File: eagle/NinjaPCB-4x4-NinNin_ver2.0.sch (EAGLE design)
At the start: 72 parts, among them IC3 ANALOGSW_AD_SOT23-6, IC6 NAU7802, J2 ATX24, J3 HEATER, J4 HEATER_TEMP, Q1 S8550, Q2 IRF520NPBF, Q3 IRF520NPBF, Q4 S8550, Q5 IRF520NPBF, Q6 S8550, Q7 S8550, Q8 S8550, U1 CJT1117-3.3-SOT223

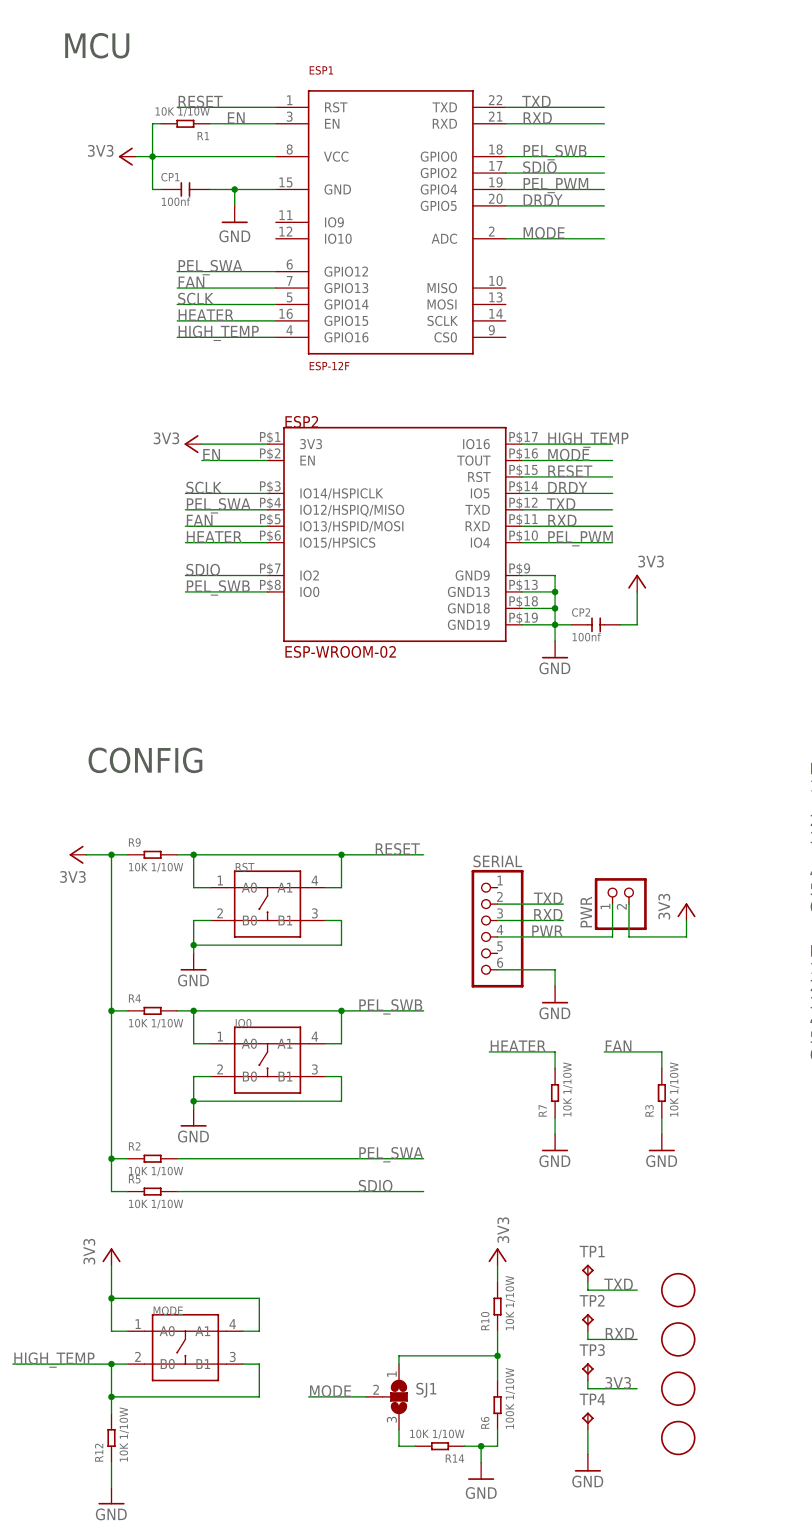
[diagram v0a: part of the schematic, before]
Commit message: abstract layout image of 2x2MooMoo
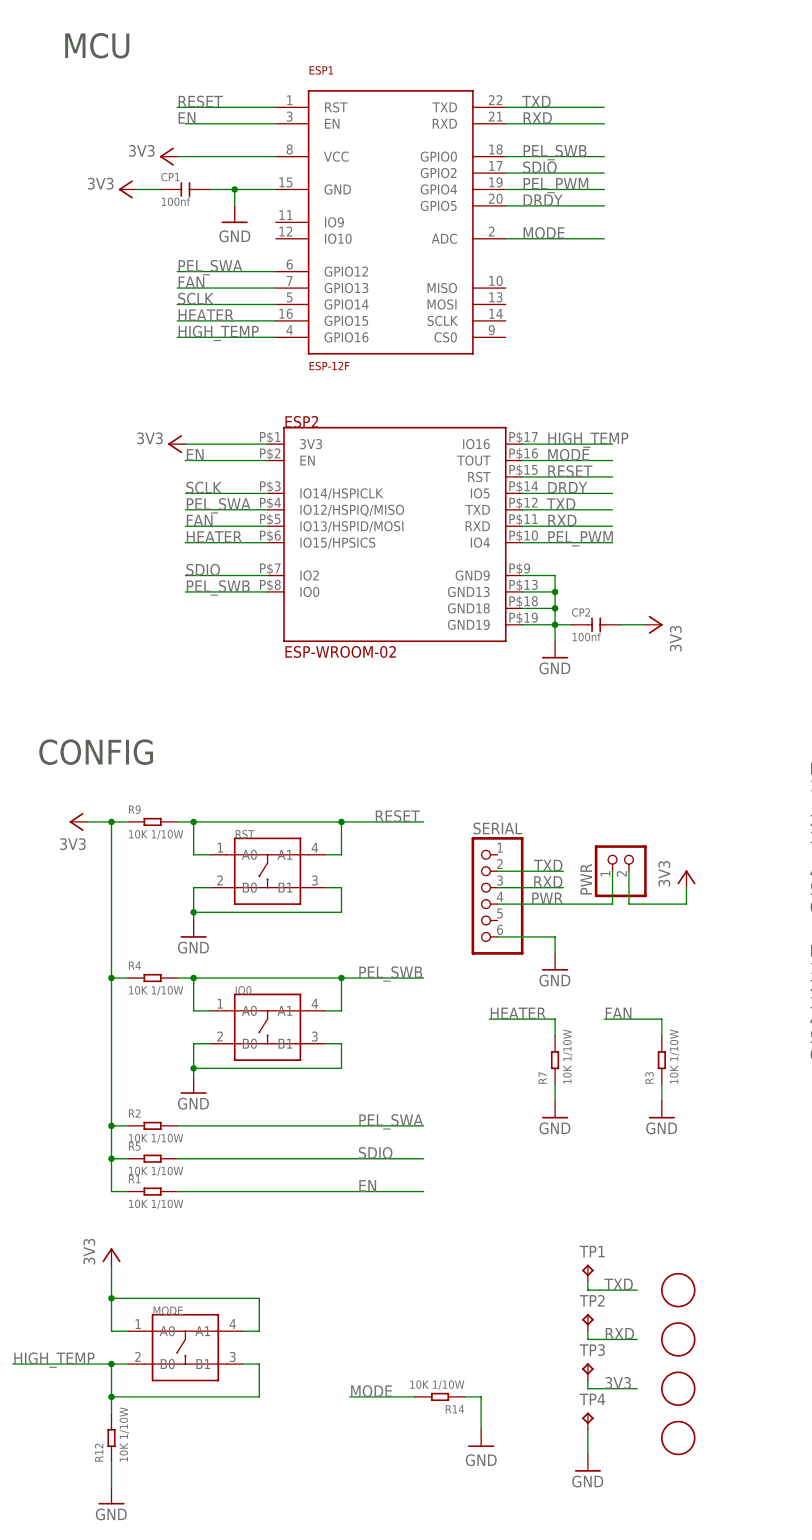
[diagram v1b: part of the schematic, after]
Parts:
- removed R10: 10K 1/10W, Seeed-Resistor:SMD-RES-10K-5%-1/10W(0603)
- removed R6: 100K 1/10W, Seeed-Resistor:SMD-RES-100K-5%-1/10W(0603)
- removed SJ1: (no value), jumper:SJ2W
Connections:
- removed net N$8: R10.1, R6.2, SJ1.1
- removed net N$9: R14.2, SJ1.3
- net 3V3: now also R1.1; no longer R1.2, R10.2
- net EN: now also R1.2; no longer R1.1
- net GND: no longer R6.1
- net MODE: now also R14.2; no longer SJ1.2
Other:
- moved on the sheet: IO0, PWR, R1, R14, R2, R3, R4, R5, R7, R9, RST, SERIAL

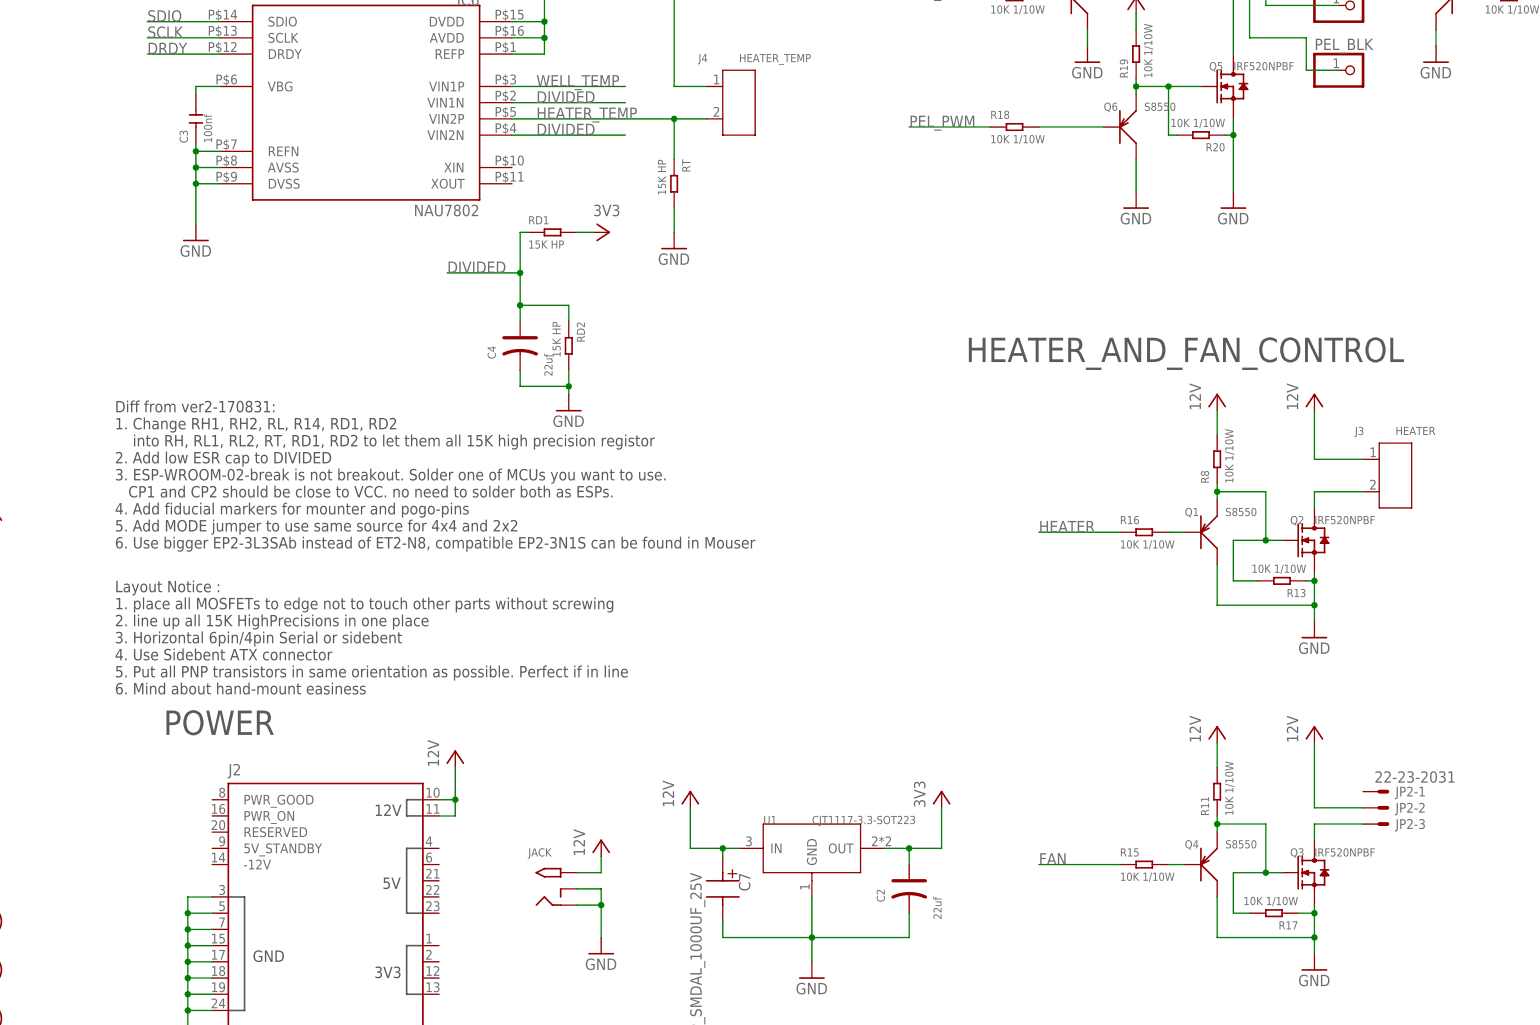
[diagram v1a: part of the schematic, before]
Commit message: change values of MOSFET G-S reg
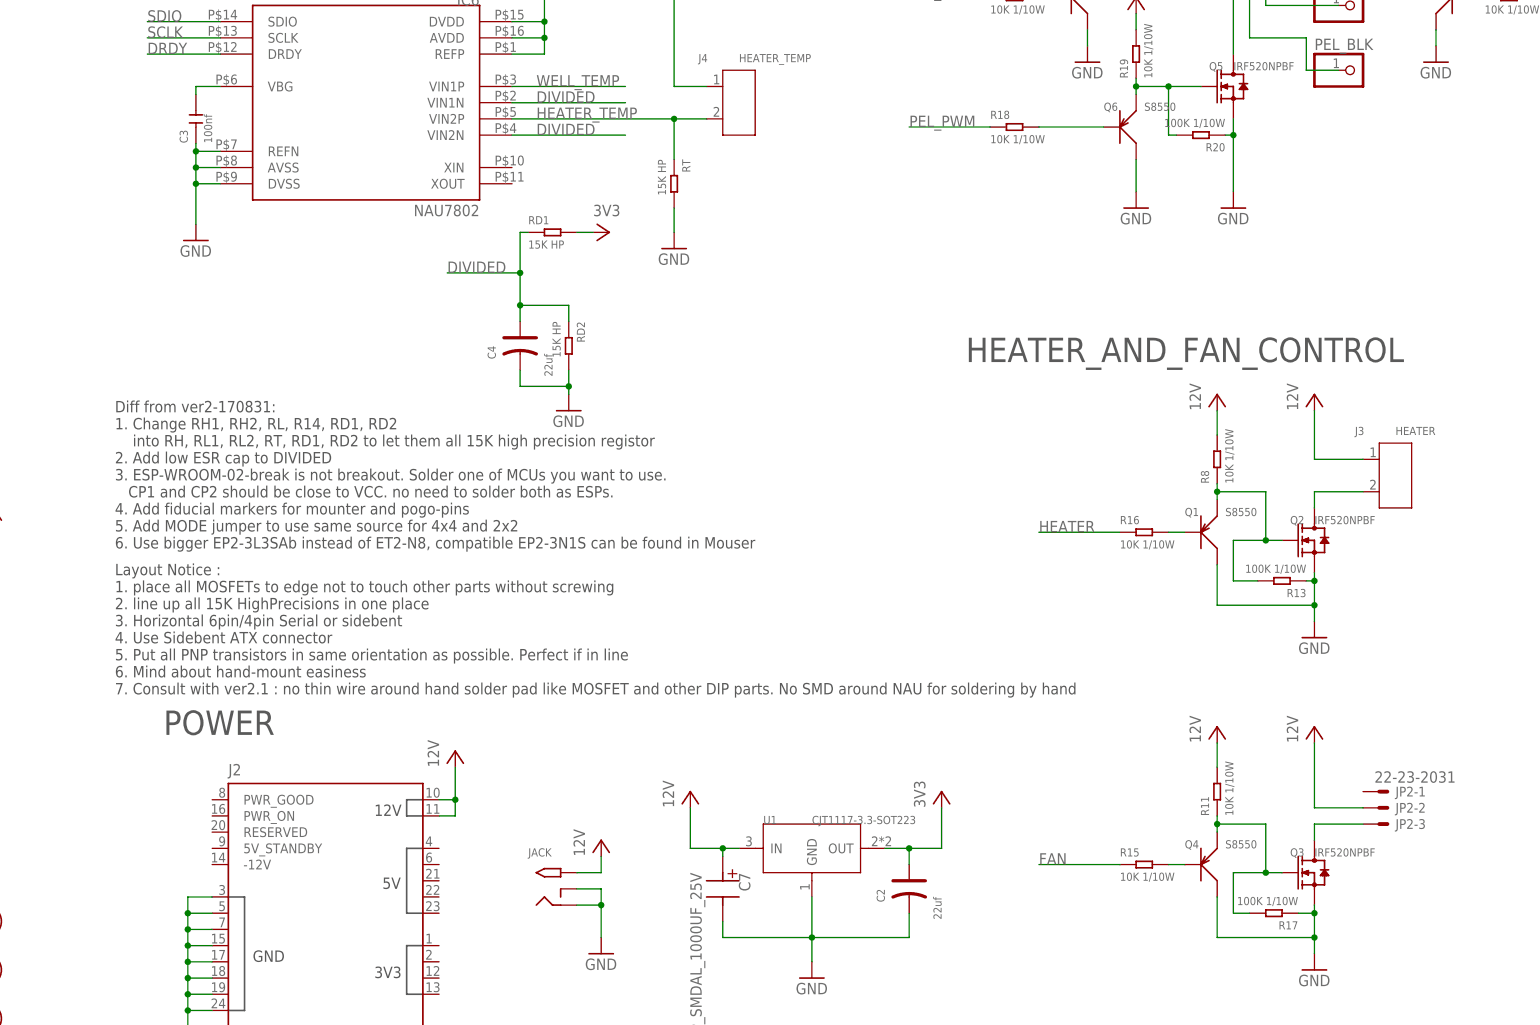
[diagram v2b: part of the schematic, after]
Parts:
- R13, R17, R20: value 10K 1/10W -> 100K 1/10W; device Seeed-Resistor:SMD-RES-10K-5%-1/10W(0603) -> Seeed-Resistor:SMD-RES-100K-5%-1/10W(0603)
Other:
- note added: "Layout Notice : 1. place all MOSFETs to edge not to touch other parts without screwing 2. line up all 15K HighPrecisions in one place 3. Horizontal 6pin/4pin Serial or sidebent 4. Use Sidebent ATX connector 5. Put all PNP transistors in same orientation as possible. Perfect if in line 6. Mind about hand-mount easiness 7. Consult with ver2.1 : no thin wire around hand solder pad like MOSFET and ot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"
- note removed: "Layout Notice : 1. place all MOSFETs to edge not to touch other parts without screwing 2. line up all 15K HighPrecisions in one place 3. Horizontal 6pin/4pin Serial or sidebent 4. Use Sidebent ATX connector 5. Put all PNP transistors in same orientation as possible. Perfect if in line 6. Mind about hand-mount easiness"
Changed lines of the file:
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@@
 <setting verticaltext="up"/>
 </settings>
-<grid distance="0.05" unitdist="inch" unit="inch" style="lines" multiple="1" display="no" altdistance="0.01" altunitdist="inch" altunit="inch"/>
+<grid distance="0.1" unitdist="inch" unit="inch" style="lines" multiple="1" display="no" altdistance="0.01" altunitdist="inch" altunit="inch"/>
 <layers>
 <layer number="1" name="Top" color="4" fill="1" visible="no" active="no"/>
@@
 <part name="R8" library="Seeed-Resistor" deviceset="SMD-RES-10K-5%-1/10W(0603)" device="" value="10K 1/10W"/>
 <part name="R11" library="Seeed-Resistor" deviceset="SMD-RES-10K-5%-1/10W(0603)" device="" value="10K 1/10W"/>
-<part name="R13" library="Seeed-Resistor" deviceset="SMD-RES-10K-5%-1/10W(0603)" device="" value="10K 1/10W"/>
-<part name="R17" library="Seeed-Resistor" deviceset="SMD-RES-10K-5%-1/10W(0603)" device="" value="10K 1/10W"/>
+<part name="R13" library="Seeed-Resistor" deviceset="SMD-RES-100K-5%-1/10W(0603)" device="" value="100K 1/10W"/>
+<part name="R17" library="Seeed-Resistor" deviceset="SMD-RES-100K-5%-1/10W(0603)" device="" value="100K 1/10W"/>
 <part name="Q5" library="Seeed-Transistor" deviceset="DIP-MOSFET-N-CH-100V-9.7A-IRF520NPBF(TO-220AB)" device="CORRECT" value="IRF520NPBF"/>
 <part name="GND3" library="supply1" deviceset="GND" device=""/>
@@
 <part name="Q6" library="Seeed-Transistor" deviceset="SMD-TRANSISTORS-PNP-25V-500MA-S8550(SOT-23)" device="" value="S8550"/>
 <part name="R19" library="Seeed-Resistor" deviceset="SMD-RES-10K-5%-1/10W(0603)" device="" value="10K 1/10W"/>
-<part name="R20" library="Seeed-Resistor" deviceset="SMD-RES-10K-5%-1/10W(0603)" device="" value="10K 1/10W"/>
+<part name="R20" library="Seeed-Resistor" deviceset="SMD-RES-100K-5%-1/10W(0603)" device="" value="100K 1/10W"/>
 <part name="RELAY" library="PCR-Switch" deviceset="NEC-RELAY2" device="EP2" value="NEC-RELAY2EP2"/>
 <part name="D1" library="Seeed-Diode" deviceset="DIODE-GEN-PURPOSE-1KV-1A(DO-214AC)" device="" value="1N4007"/>
@@
 4. Use Sidebent ATX connector
 5. Put all PNP transistors in same orientation as possible. Perfect if in line
-6. Mind about hand-mount easiness</text>
+6. Mind about hand-mount easiness
+7. Consult with ver2.1 : no thin wire around hand solder pad like MOSFET and other DIP parts. No SMD around NAU for soldering by hand</text>
 </plain>
 <instances>

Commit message: start wiring NinNin ver2.0
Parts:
- removed PWR: (no value), pinhead:PINHD-1X2
- removed Q3, Q5: IRF520NPBF, Seeed-Transistor:DIP-MOSFET-N-CH-100V-9.7A-IRF520NPBF(TO-220AB)CORRECT
- removed Q6, Q7, Q8: S8550, Seeed-Transistor:SMD-TRANSISTORS-PNP-25V-500MA-S8550(SOT-23)
- removed R11, R8: 10K 1/10W, Seeed-Resistor:SMD-RES-10K-5%-1/10W(0603)
- removed SERIAL: (no value), pinhead:PINHD-1X6
- added ESP3: ESP-WROOM-02-BREAK, PCR-Module:ESP-WROOM-02-BREAK
- added FAN_ON: (no value), jumper:SJ
- added Q10, Q11, Q9: S9013, Seeed-Transistor:SMD-TRANSISTORS-NPN-25V-500MA-S9013(SOT-23)
- added SERIAL4: (no value), pinhead:PINHD-1X4
- added SERIAL6: (no value), pinhead:PINHD-1X6
- added TP5, TP6, TP7: TPTP20R, testpad:TPTP20R
- added U$1: HEAT111PB015, PCR-Connector:HEAT111PB015
- J2: value ATX24 -> ATX24NH; device PCR-Connector:ATX24 -> PCR-Connector:ATX24NH
- Q1, Q4: value S8550 -> CJ2302; device Seeed-Transistor:SMD-TRANSISTORS-PNP-25V-500MA-S8550(SOT-23) -> Seeed-Transistor:SMD-MOSFET-N-CH-20V-2.1A-CJ2302(SOT-23)
- Q2: value IRF520NPBF -> IRLB3813PBF; device Seeed-Transistor:DIP-MOSFET-N-CH-100V-9.7A-IRF520NPBF(TO-220AB)CORRECT -> transistor-power:IRF520
- R13, R17, R20: value 100K 1/10W -> 10K 1/10W; device Seeed-Resistor:SMD-RES-100K-5%-1/10W(0603) -> Seeed-Resistor:SMD-RES-10K-5%-1/10W(0603)
- R15, R16, R18: value 10K 1/10W -> 1K 1/10W; device Seeed-Resistor:SMD-RES-10K-5%-1/10W(0603) -> Seeed-Resistor:SMD-RES-1K-5%-1/10W(0603)
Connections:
- removed net N$25: Q3.G, Q4.E, R11.1, R17.2
- removed net N$29: Q1.E, Q2.G, R13.2, R8.1
- removed net N$31: Q4.B, R15.2
- removed net PWR: PWR.1, SERIAL.4
- new net N$8: Q4.G, R15.2, R17.2
- net 12V: no longer R11.2, R8.2
- net 3V3: now also ESP3.3V3, SERIAL4.1, SERIAL6.4; no longer PWR.2, R2.1
- net DRDY: now also ESP3.IO5
- net EN: now also ESP3.EN
- net FAN: now also ESP1.GPIO0, ESP2.IO0, ESP3.IO0, IO0.A0, IO0.A1, R4.2, TP5.TP; no longer ESP1.GPIO13, ESP2.IO13/HSPID/MOSI, R3.2
- net GND: now also ESP3.GND13, ESP3.GND18, ESP3.GND9, FAN_ON.1, Q1.S, Q10.E, Q11.E, Q4.S, Q9.E, R2.1, SERIAL4.4, SERIAL6.6; no longer Q1.C, Q3.S, Q4.C, Q5.S, Q6.C, Q7.C, Q8.C, SERIAL.6
- net HEATER: now also ESP3.IO15/HPSICS
- net HIGH_TEMP: now also ESP3.IO16, TP7.TP
- net MODE: now also ESP3.TOUT
- net N$2: now also Q1.D; no longer Q2.D
- net N$3: now also Q2.D; no longer Q5.D
- net N$30: now also Q11.B; no longer Q6.B
- net N$32: now also Q1.G, R13.2; no longer Q1.B
- net N$33: now also Q9.C; no longer Q7.E
- net N$34: now also Q9.B; no longer Q7.B
- net N$35: now also Q10.B; no longer Q8.B
- net N$36: now also Q10.C; no longer Q8.E
- net N$4: now also FAN_ON.2, Q4.D; no longer Q3.D
- net N$5: now also Q11.C, Q2.G; no longer Q5.G, Q6.E
- net PEL_PWM: now also ESP3.IO4
- net PEL_SWA: now also ESP3.IO12/HSPIQ/MISO
- net PEL_SWB: now also ESP1.GPIO13, ESP2.IO13/HSPID/MOSI, ESP3.IO13/HSPID/MOSI, R3.2; no longer ESP1.GPIO0, ESP2.IO0, IO0.A0, IO0.A1, R4.2
- net RESET: now also ESP3.RST, TP6.TP
- net RXD: now also ESP3.RXD, SERIAL4.2, SERIAL6.3; no longer SERIAL.3
- net SCLK: now also ESP3.IO14/HSPICLK
- net SDIO: now also ESP3.IO2
- net TXD: now also ESP3.TXD, SERIAL4.3, SERIAL6.2; no longer SERIAL.2
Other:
- note added: "Layout Notice : 1. line up all 15K HighPrecisions in one place 2. Horizontal 6pin/4pin Serial or sidebent 3. Use Sidebent ATX connector 4. Put all PNP transistors in same orientation as possible. Perfect if in line 5. Mind about hand-mount easiness 6. Consult with ver2.1 : no thin wire around hand solder pad like MOSFET and other DIP parts. No SMD around NAU for soldering by hand 7. Let Fan short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"
- note removed: "Layout Notice : 1. place all MOSFETs to edge not to touch other parts without screwing 2. line up all 15K HighPrecisions in one place 3. Horizontal 6pin/4pin Serial or sidebent 4. Use Sidebent ATX connector 5. Put all PNP transistors in same orientation as possible. Perfect if in line 6. Mind about hand-mount easiness 7. Consult with ver2.1 : no thin wire around hand solder pad like MOSFET and ot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"
- moved on the sheet: C3, C4, IC3, IC6, J4, JP2-1, JP2-2, JP2-3, R13, R14, R15, R16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

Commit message: wired
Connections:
- net N$3: now also U$1.P$1
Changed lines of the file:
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@@
 <setting verticaltext="up"/>
 </settings>
-<grid distance="0.1" unitdist="inch" unit="inch" style="lines" multiple="1" display="no" altdistance="0.01" altunitdist="inch" altunit="inch"/>
+<grid distance="0.05" unitdist="inch" unit="inch" style="lines" multiple="1" display="no" altdistance="0.01" altunitdist="inch" altunit="inch"/>
 <layers>
 <layer number="1" name="Top" color="4" fill="1" visible="yes" active="no"/>
@@
 <instance part="3V11" gate="VCC" x="125.73" y="121.92"/>
 <instance part="SERIAL4" gate="A" x="113.03" y="109.22" rot="MR0"/>
-<instance part="U$1" gate="G$1" x="331.47" y="168.91"/>
+<instance part="U$1" gate="G$1" x="312.42" y="189.23" rot="R180"/>
 <instance part="Q2" gate="G$1" x="314.96" y="181.61" smashed="yes">
 <attribute name="NAME" x="318.77" y="176.53" size="1.778" layer="95"/>
@@
 <net name="N$3" class="0">
 <segment>
-<wire x1="317.5" y1="196.85" x2="317.5" y2="186.69" width="0.1524" layer="91"/>
+<wire x1="317.5" y1="196.85" x2="317.5" y2="189.23" width="0.1524" layer="91"/>
 <pinref part="RELAY" gate="G$1" pin="5"/>
 <pinref part="Q2" gate="G$1" pin="D"/>
-</segment>
-</net>
+<wire x1="317.5" y1="189.23" x2="317.5" y2="186.69" width="0.1524" layer="91"/>
+<wire x1="314.96" y1="189.23" x2="317.5" y2="189.23" width="0.1524" layer="91"/>
+<junction x="317.5" y="189.23"/>
+<pinref part="U$1" gate="G$1" pin="P$1"/>
+</segment>
+</net>
